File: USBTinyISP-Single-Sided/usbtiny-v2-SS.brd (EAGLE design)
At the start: 56.8 x 33 mm, 23 parts, among them IC1 ATTINY2313-20P, IC2 74AHC125N, Q1 12Mhz, X1 USB_CONN

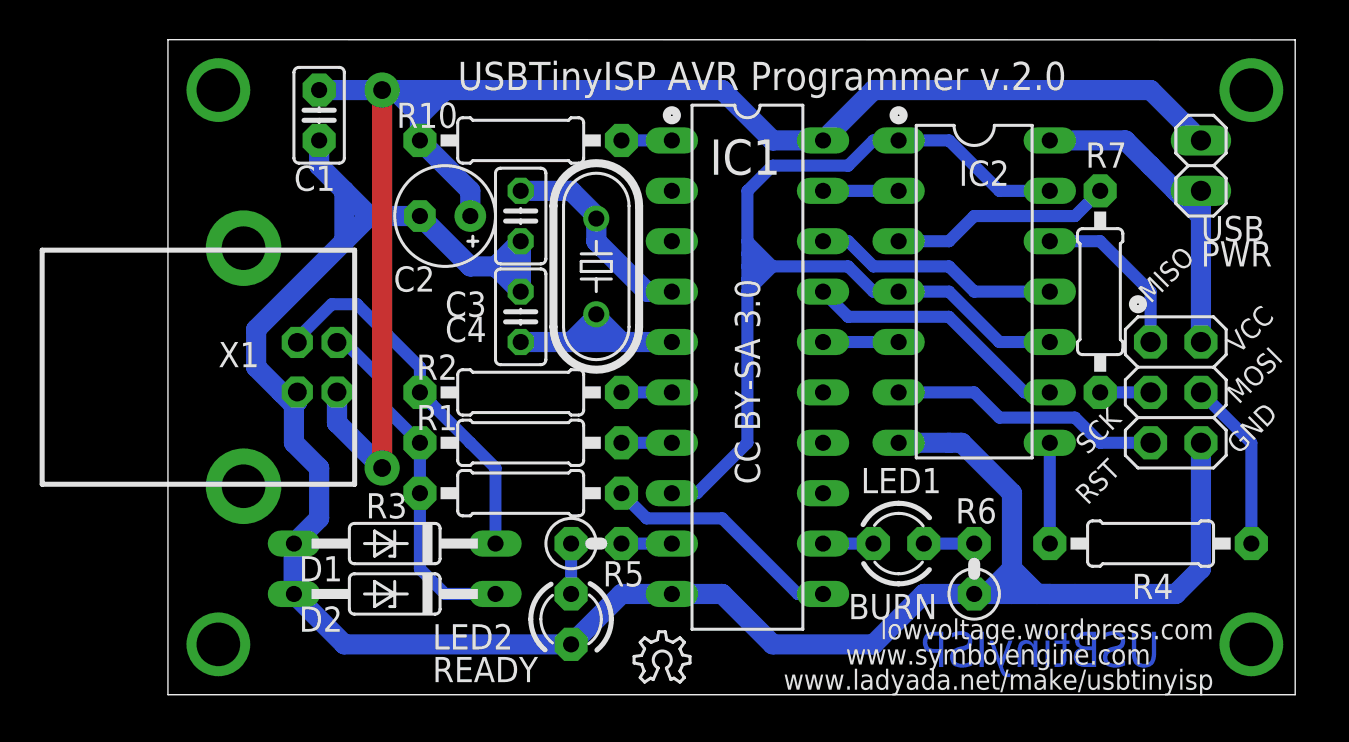
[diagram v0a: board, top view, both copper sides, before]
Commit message: Add PCB version. Optimize wires. Fix jumper clearance
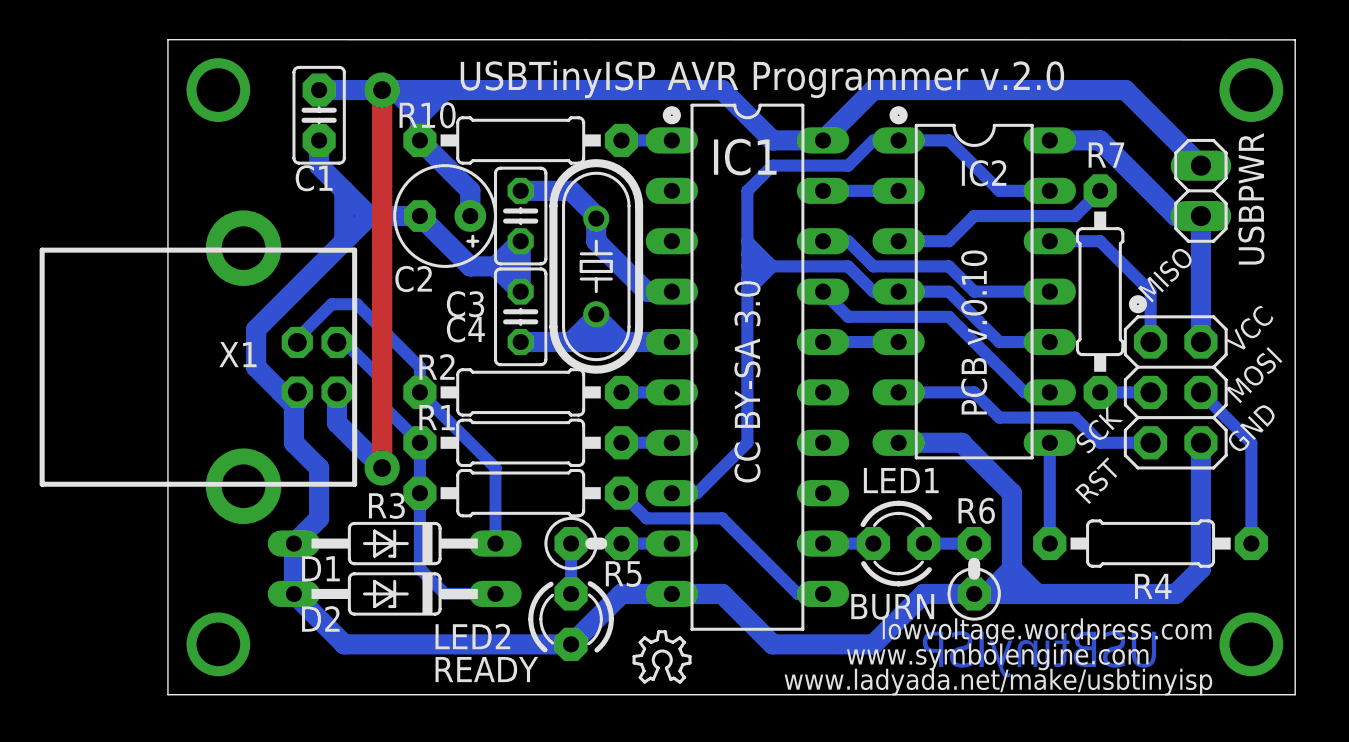
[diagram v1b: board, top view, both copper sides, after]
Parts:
- moved JP3 1.27 mm to (52.1, 25.4)
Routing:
- net GND: track 135.6 -> 119.2 mm
- net VCC_REMOTE: track 18.1 -> 15.5 mm
- net VCC: track 84.0 -> 82.9 mm
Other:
- board text added: "PCB v.0.10"
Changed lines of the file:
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@@
 <text x="49.53" y="19.685" size="1.016" layer="21" rot="R45">MISO</text>
 <circle x="48.895" y="19.685" radius="0.254" width="0.4064" layer="21"/>
-<text x="52.07" y="22.86" size="1.27" layer="21">USB</text>
-<text x="52.07" y="21.59" size="1.27" layer="21">PWR</text>
+<text x="53.975" y="24.765" size="1.27" layer="21" rot="R270">USB</text>
+<text x="55.245" y="24.765" size="1.27" layer="21" rot="R90">PWR</text>
 <text x="14.605" y="30.48" size="1.4224" layer="21">USBTinyISP AVR Programmer v.2.0</text>
 <text x="46.355" y="12.065" size="1.016" layer="21" rot="R45">SCK</text>
@@
 <circle x="25.4" y="29.21" radius="0.254" width="0.4064" layer="21"/>
 <circle x="36.83" y="29.21" radius="0.254" width="0.4064" layer="21"/>
+<text x="41.275" y="13.97" size="1.27" layer="21" rot="R90">PCB v.0.10</text>
 </plain>
 <attributes>
@@
 <attribute name="VALUE" x="28.448" y="26.67" size="1.778" layer="27" ratio="10" rot="R270"/>
 </element>
-<element name="JP3" library="pinhead" package="1X02" value="PWR_JUMPER" x="52.07" y="26.67" smashed="yes" rot="R90">
-<attribute name="NAME" x="48.1838" y="29.1338" size="1.27" layer="25" ratio="10" display="off"/>
-<attribute name="VALUE" x="55.245" y="24.13" size="1.27" layer="27" rot="R90"/>
+<element name="JP3" library="pinhead" package="1X02" value="PWR_JUMPER" x="52.07" y="25.4" smashed="yes" rot="R90">
+<attribute name="NAME" x="48.1838" y="27.8638" size="1.27" layer="25" ratio="10" display="off"/>
+<attribute name="VALUE" x="55.245" y="22.86" size="1.27" layer="27" rot="R90"/>
 </element>
 <element name="C1" library="rcl-ez" package="C025-025X050" value="0.1uF" x="7.62" y="29.21" smashed="yes" rot="R270">
@@
 <contactref element="D1" pad="C"/>
 <contactref element="X1" pad="3"/>
-<wire x1="12.7" y1="15.24" x2="13.335" y2="14.605" width="0.6096" layer="16"/>
-<wire x1="13.335" y1="14.605" x2="15.24" y2="12.7" width="0.6096" layer="16"/>
+<wire x1="12.7" y1="15.24" x2="16.51" y2="11.43" width="0.6096" layer="16"/>
 <wire x1="16.51" y1="7.62" x2="16.51" y2="11.43" width="0.6096" layer="16"/>
-<wire x1="16.51" y1="11.43" x2="15.24" y2="12.7" width="0.6096" layer="16"/>
 <wire x1="6.52" y1="17.76" x2="6.52" y2="17.95" width="0.6096" layer="16"/>
 <wire x1="6.52" y1="17.95" x2="8.255" y2="19.685" width="0.6096" layer="16"/>
@@
 <wire x1="12.7" y1="29.21" x2="12.7" y2="30.48" width="1.016" layer="16"/>
 <wire x1="33.02" y1="27.94" x2="35.56" y2="30.48" width="1.016" layer="16"/>
-<wire x1="35.56" y1="30.48" x2="49.53" y2="30.48" width="1.016" layer="16"/>
-<wire x1="49.53" y1="30.48" x2="52.07" y2="27.94" width="1.016" layer="16"/>
+<wire x1="35.56" y1="30.48" x2="48.26" y2="30.48" width="1.016" layer="16"/>
+<wire x1="48.26" y1="30.48" x2="52.07" y2="26.67" width="1.016" layer="16"/>
 <wire x1="12.7" y1="27.94" x2="15.24" y2="25.4" width="1.016" layer="16"/>
 <wire x1="15.24" y1="25.4" x2="15.24" y2="24.13" width="1.016" layer="16"/>
 <wire x1="11.43" y1="30.48" x2="12.7" y2="29.21" width="1.016" layer="16"/>
 <wire x1="12.7" y1="29.21" x2="13.97" y2="30.48" width="1.016" layer="16"/>
-<wire x1="8.52" y1="15.26" x2="8.52" y2="13.705" width="1.016" layer="16"/>
 <wire x1="7.62" y1="30.48" x2="10.795" y2="30.48" width="1.016" layer="16"/>
 <wire x1="8.52" y1="15.26" x2="8.52" y2="13.705" width="1.016" layer="16"/>
@@
 <contactref element="C3" pad="2"/>
 <contactref element="C4" pad="2"/>
-<wire x1="17.78" y1="22.86" x2="17.78" y2="20.32" width="1.016" layer="16"/>
 <wire x1="7.62" y1="11.43" x2="7.62" y2="8.89" width="1.016" layer="16"/>
 <wire x1="7.62" y1="8.89" x2="6.35" y2="7.62" width="1.016" layer="16"/>
 <wire x1="6.35" y1="7.62" x2="6.35" y2="5.08" width="1.016" layer="16"/>
-<wire x1="6.35" y1="5.08" x2="6.35" y2="7.62" width="1.016" layer="16"/>
-<wire x1="6.35" y1="5.08" x2="6.35" y2="7.62" width="0.6096" layer="16"/>
-<wire x1="6.35" y1="7.62" x2="6.35" y2="5.08" width="1.016" layer="16"/>
-<wire x1="36.83" y1="12.7" x2="39.37" y2="12.7" width="1.016" layer="16"/>
-<wire x1="44.45" y1="5.08" x2="45.72" y2="5.08" width="1.016" layer="16"/>
-<wire x1="45.72" y1="5.08" x2="50.8" y2="5.08" width="1.016" layer="16"/>
+<wire x1="36.83" y1="12.7" x2="40.005" y2="12.7" width="1.016" layer="16"/>
+<wire x1="44.45" y1="5.08" x2="50.8" y2="5.08" width="1.016" layer="16"/>
 <wire x1="50.8" y1="5.08" x2="52.07" y2="6.35" width="1.016" layer="16"/>
-<wire x1="52.07" y1="6.35" x2="52.07" y2="8.89" width="1.016" layer="16"/>
-<wire x1="52.07" y1="8.89" x2="52.07" y2="12.7" width="1.016" layer="16"/>
+<wire x1="52.07" y1="6.35" x2="52.07" y2="12.7" width="1.016" layer="16"/>
 <wire x1="25.4" y1="5.08" x2="27.94" y2="5.08" width="1.016" layer="16"/>
 <wire x1="27.94" y1="5.08" x2="30.48" y2="2.54" width="1.016" layer="16"/>
 <wire x1="30.48" y1="2.54" x2="35.56" y2="2.54" width="1.016" layer="16"/>
-<wire x1="41.91" y1="5.08" x2="42.545" y2="5.08" width="1.016" layer="16"/>
 <wire x1="42.545" y1="5.08" x2="43.18" y2="5.08" width="1.016" layer="16"/>
-<wire x1="43.18" y1="5.08" x2="43.815" y2="5.08" width="1.016" layer="16"/>
-<wire x1="43.815" y1="5.08" x2="44.45" y2="5.08" width="1.016" layer="16"/>
 <wire x1="12.7" y1="24.13" x2="15.24" y2="21.59" width="1.016" layer="16"/>
 <wire x1="15.24" y1="21.59" x2="16.51" y2="21.59" width="1.016" layer="16"/>
-<wire x1="16.51" y1="21.59" x2="17.78" y2="21.59" width="1.016" layer="16"/>
 <wire x1="17.78" y1="21.59" x2="16.51" y2="21.59" width="1.016" layer="16"/>
 <wire x1="16.51" y1="21.59" x2="17.78" y2="20.32" width="1.016" layer="16"/>
 <wire x1="17.78" y1="20.32" x2="17.78" y2="22.86" width="1.016" layer="16"/>
-<wire x1="41.91" y1="5.08" x2="41.275" y2="5.08" width="1.016" layer="16"/>
-<wire x1="41.275" y1="5.08" x2="40.64" y2="5.08" width="1.016" layer="16"/>
 <wire x1="40.64" y1="5.08" x2="38.1" y2="5.08" width="1.016" layer="16"/>
 <wire x1="38.1" y1="5.08" x2="35.56" y2="2.54" width="1.016" layer="16"/>
@@
 <wire x1="43.18" y1="5.08" x2="43.815" y2="5.08" width="1.016" layer="16"/>
 <wire x1="43.815" y1="5.08" x2="44.45" y2="5.08" width="1.016" layer="16"/>
-<wire x1="39.37" y1="12.7" x2="40.005" y2="12.7" width="1.016" layer="16"/>
 <wire x1="40.005" y1="12.7" x2="42.545" y2="10.16" width="1.016" layer="16"/>
 <wire x1="42.545" y1="10.16" x2="42.545" y2="6.35" width="1.016" layer="16"/>
@@
 <wire x1="8.89" y1="25.4" x2="10.16" y2="24.13" width="1.016" layer="16"/>
 <wire x1="8.89" y1="25.4" x2="8.89" y2="22.86" width="1.016" layer="16"/>
-<wire x1="42.545" y1="6.35" x2="43.815" y2="5.08" width="1.016" layer="16"/>
 <wire x1="43.815" y1="5.08" x2="42.545" y2="6.35" width="1.016" layer="16"/>
 <wire x1="42.545" y1="6.35" x2="41.275" y2="5.08" width="1.016" layer="16"/>
@@
 <contactref element="JP3" pad="1"/>
 <contactref element="IC2" pad="14"/>
-<wire x1="52.07" y1="25.4" x2="50.8" y2="25.4" width="1.016" layer="16"/>
-<wire x1="50.8" y1="25.4" x2="49.53" y2="26.67" width="1.016" layer="16"/>
-<wire x1="49.53" y1="26.67" x2="48.26" y2="27.94" width="1.016" layer="16"/>
-<wire x1="48.26" y1="27.94" x2="44.45" y2="27.94" width="1.016" layer="16"/>
-<wire x1="52.07" y1="25.4" x2="52.07" y2="24.13" width="1.016" layer="16"/>
+<wire x1="50.8" y1="24.13" x2="46.99" y2="27.94" width="1.016" layer="16"/>
+<wire x1="46.99" y1="27.94" x2="44.45" y2="27.94" width="1.016" layer="16"/>
 <wire x1="52.07" y1="24.13" x2="52.07" y2="17.78" width="1.016" layer="16"/>
-<wire x1="50.8" y1="25.4" x2="52.07" y2="24.13" width="1.016" layer="16"/>
+<wire x1="50.8" y1="24.13" x2="52.07" y2="24.13" width="1.016" layer="16"/>
 </signal>
 <signal name="RST'">

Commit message: Fixed board dimensions
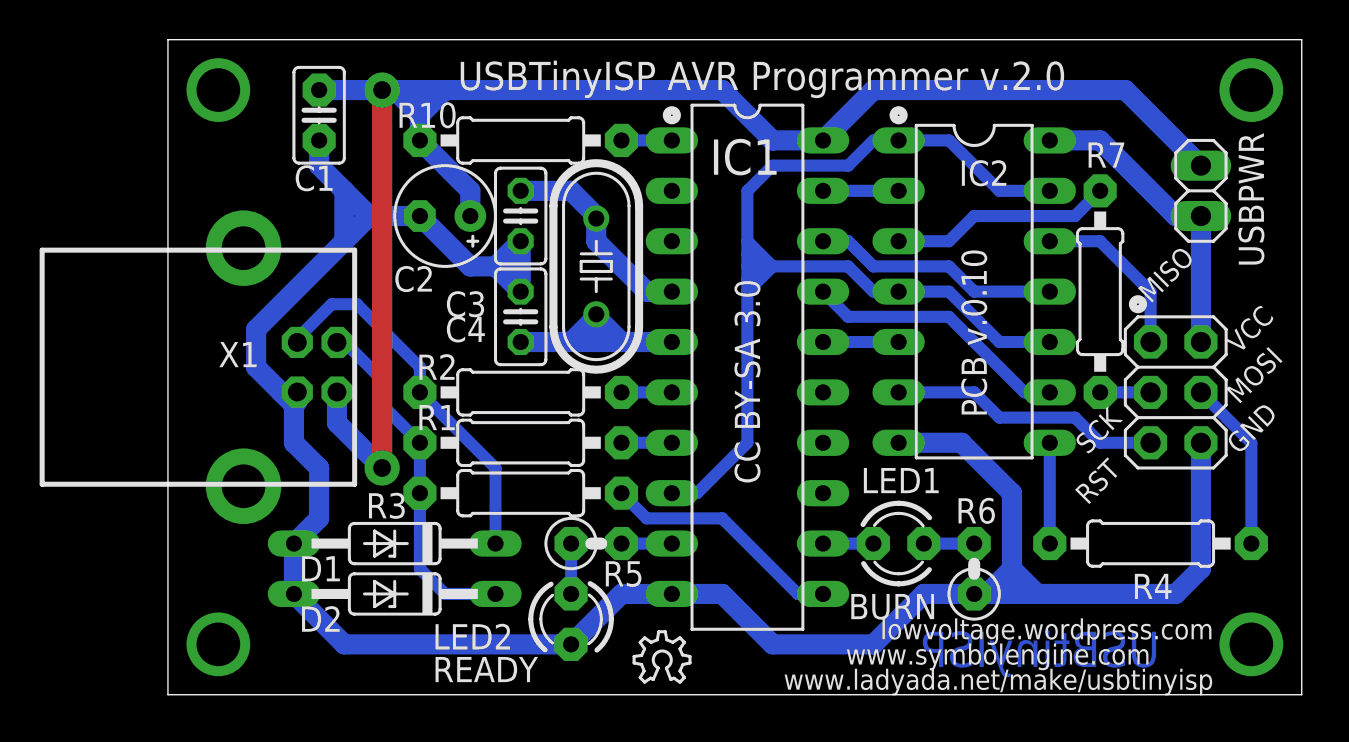
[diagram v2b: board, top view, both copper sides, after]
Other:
- board size 56.8 x 33 mm -> 57.1 x 33 mm
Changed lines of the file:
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@@
 <board>
 <plain>
-<wire x1="0" y1="0" x2="56.82" y2="0" width="0" layer="20"/>
-<wire x1="56.82" y1="0" x2="56.82" y2="33.01" width="0" layer="20"/>
-<wire x1="56.82" y1="33.01" x2="0" y2="33.02" width="0" layer="20"/>
+<wire x1="0" y1="0" x2="57.15" y2="0" width="0" layer="20"/>
+<wire x1="57.15" y1="0" x2="57.15" y2="33.02" width="0" layer="20"/>
+<wire x1="57.15" y1="33.02" x2="0" y2="33.02" width="0" layer="20"/>
 <wire x1="0" y1="33.02" x2="0" y2="0" width="0" layer="20"/>
 <text x="37.973" y="3.175" size="1.778" layer="16" font="vector" ratio="15" rot="MR180">USBtinyISP</text>
